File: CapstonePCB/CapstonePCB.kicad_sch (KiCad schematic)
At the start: 29 parts, among them J1 Conn_02x40_Counter_Clockwise, J2 Barrel_Jack, U1 NUCLEO64-F411RE, U2 LP-MSPM0G3507, U3 STSPIN220, U4 SN74AHC14N, U5 LM7805_TO220, U6 TLV1117-33, U8 APDS-9306

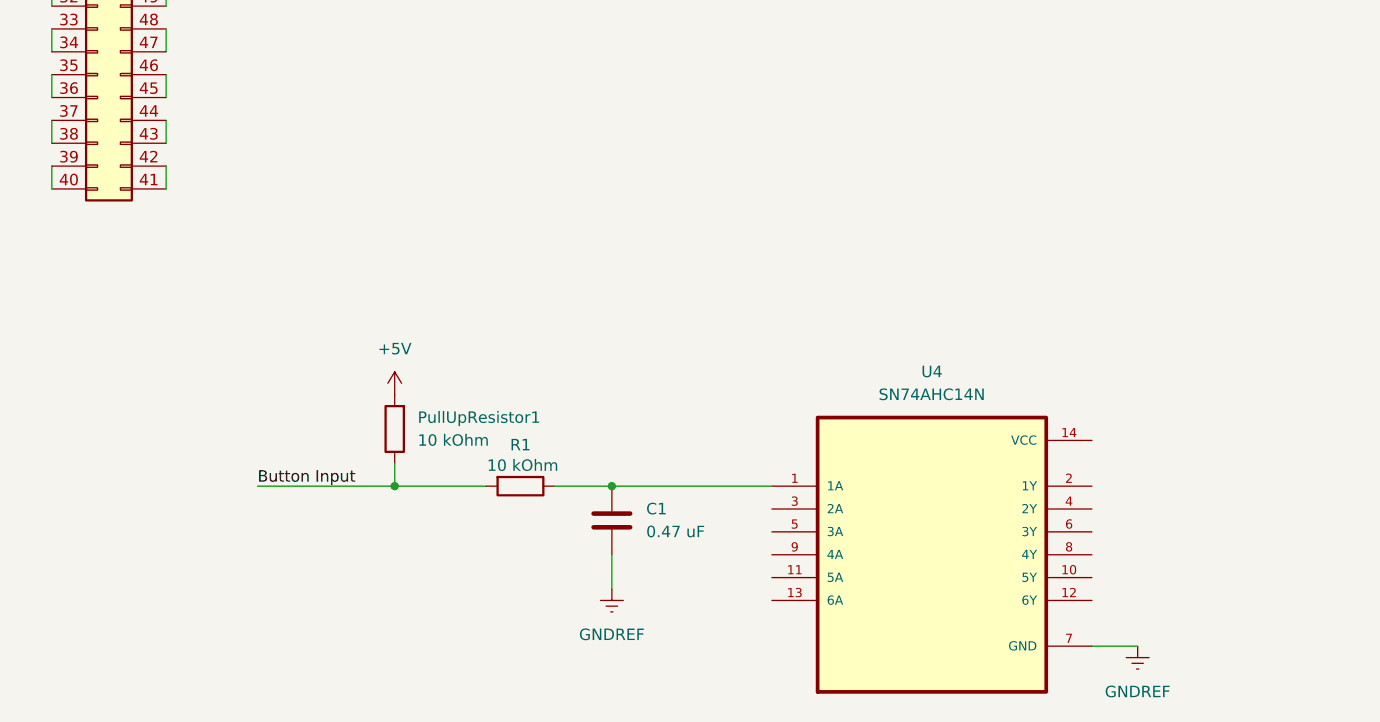
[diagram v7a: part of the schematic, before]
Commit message: Added a ground plane
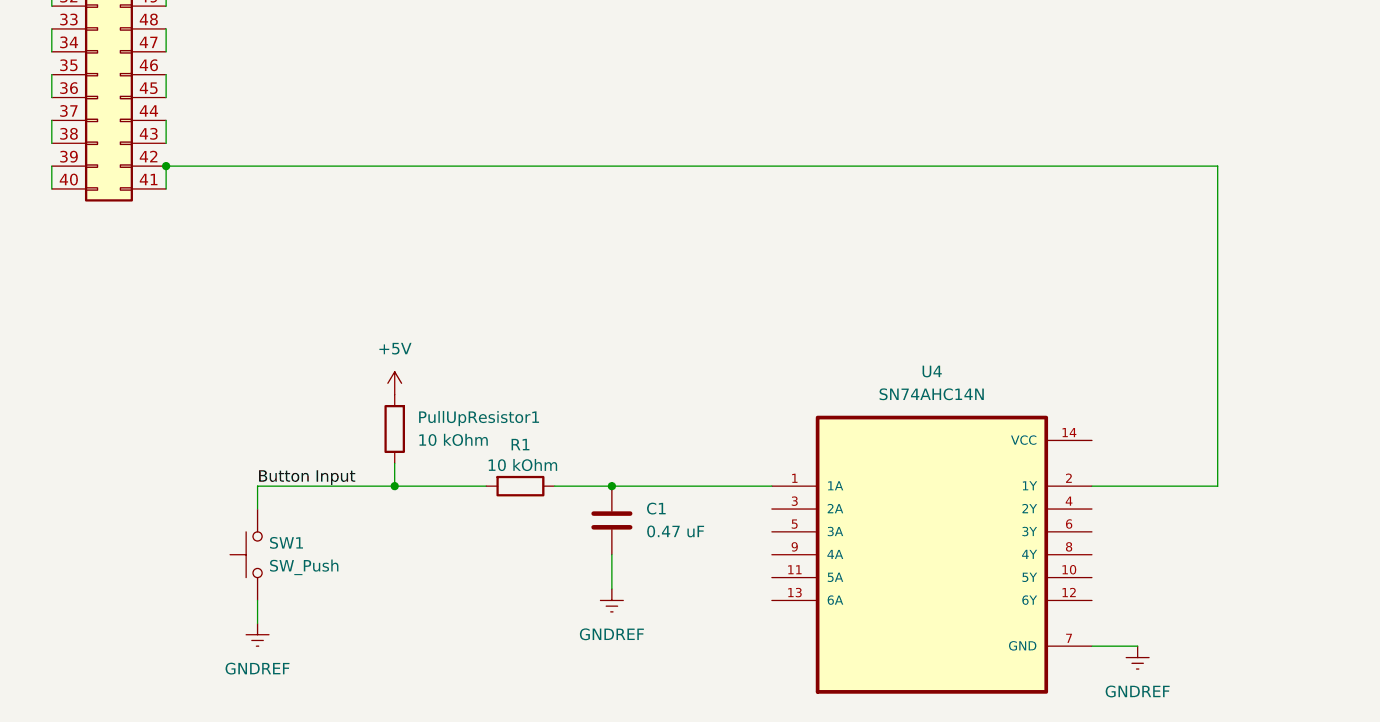
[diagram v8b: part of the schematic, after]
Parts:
- added SW1: SW_Push, Button_Switch_THT:SW_PUSH_6mm_H7.3mm, symbol Switch:SW_Push
- C1: footprint (none) -> Capacitor_SMD:C_0201_0603Metric
- PullUpResistor1, R1: footprint (none) -> Resistor_SMD:R_0201_0603Metric
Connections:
- net Button Input: now also SW1.2
- net GNDREF: now also SW1.1
- net at U4.2 (1Y): now also J1.41 (Pin_41), J1.42 (Pin_42)
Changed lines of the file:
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@@
 	)
 	(junction
+		(at 147.32 115.57)
+		(diameter 0)
+		(color 0 0 0 0)
+	)
+	(junction
 		(at 196.85 151.13)
 		(diameter 0)
@@
 	(wire
 		(pts
+			(xy 157.48 163.83) (xy 157.48 166.37)
+		)
+		(stroke
+			(width 0)
+			(type default)
+		)
+	)
+	(wire
+		(pts
 			(xy 369.57 31.75) (xy 369.57 34.29)
 		)
@@
 	(wire
 		(pts
+			(xy 250.19 151.13) (xy 264.16 151.13)
+		)
+		(stroke
+			(width 0)
+			(type default)
+		)
+	)
+	(wire
+		(pts
 			(xy 134.62 90.17) (xy 134.62 92.71)
 		)
@@
 	(wire
 		(pts
+			(xy 264.16 151.13) (xy 264.16 115.57)
+		)
+		(stroke
+			(width 0)
+			(type default)
+		)
+	)
+	(wire
+		(pts
 			(xy 172.72 148.59) (xy 172.72 151.13)
 		)
@@
 	(wire
 		(pts
+			(xy 157.48 151.13) (xy 157.48 153.67)
+		)
+		(stroke
+			(width 0)
+			(type default)
+		)
+	)
+	(wire
+		(pts
 			(xy 147.32 59.69) (xy 147.32 62.23)
 		)
@@
 	(wire
 		(pts
+			(xy 264.16 115.57) (xy 147.32 115.57)
+		)
+		(stroke
+			(width 0)
+			(type default)
+		)
+	)
+	(wire
+		(pts
 			(xy 204.47 13.97) (xy 204.47 17.78)
 		)
@@
 	)
 	(symbol
+		(lib_id "power:GNDREF")
+		(at 157.48 166.37 0)
+		(unit 1)
+		(exclude_from_sim no)
+		(in_bom yes)
+		(on_board yes)
+		(dnp no)
+		(fields_autoplaced yes)
+		(property "Reference" "#PWR030"
+			(at 157.48 172.72 0)
+			(effects
+				(font
+					(size 1.27 1.27)
+				)
+				(hide yes)
+			)
+		)
+		(property "Value" "GNDREF"
+			(at 157.48 171.45 0)
+			(effects
+				(font
+					(size 1.27 1.27)
+				)
+			)
+		)
+		(property "Footprint" ""
+			(at 157.48 166.37 0)
+			(effects
+				(font
+					(size 1.27 1.27)
+				)
+				(hide yes)
+			)
+		)
+		(property "Datasheet" ""
+			(at 157.48 166.37 0)
+			(effects
+				(font
+					(size 1.27 1.27)
+				)
+				(hide yes)
+			)
+		)
+		(property "Description" ""
+			(at 157.48 166.37 0)
+			(effects
+				(font
+					(size 1.27 1.27)
+				)
+			)
+		)
+		(pin "1"
+		)
+		(instances
+			(project "CapstonePCB"
+				(path "/39e7582f-7765-4fc9-b934-76d5b28d9065"
+					(reference "#PWR030")
+					(unit 1)
+				)
+			)
+		)
+	)
+	(symbol
 		(lib_id "Device:C_Small")
 		(at 391.16 29.21 0)
@@
 			)
 		)
-		(property "Footprint" ""
+		(property "Footprint" "Resistor_SMD:R_0201_0603Metric"
 			(at 174.498 144.78 90)
 			(effects
@@
 			)
 		)
-		(property "Footprint" ""
+		(property "Footprint" "Capacitor_SMD:C_0201_0603Metric"
 			(at 197.8152 158.75 0)
 			(effects
@@
 	)
 	(symbol
+		(lib_id "Switch:SW_Push")
+		(at 157.48 158.75 90)
+		(unit 1)
+		(exclude_from_sim no)
+		(in_bom yes)
+		(on_board yes)
+		(dnp no)
+		(fields_autoplaced yes)
+		(property "Reference" "SW1"
+			(at 158.75 157.4799 90)
+			(effects
+				(font
+					(size 1.27 1.27)
+				)
+				(justify right)
+			)
+		)
+		(property "Value" "SW_Push"
+			(at 158.75 160.0199 90)
+			(effects
+				(font
+					(size 1.27 1.27)
+				)
+				(justify right)
+			)
+		)
+		(property "Footprint" "Button_Switch_THT:SW_PUSH_6mm_H7.3mm"
+			(at 152.4 158.75 0)
+			(effects
+				(font
+					(size 1.27 1.27)
+				)
+				(hide yes)
+			)
+		)
+		(property "Datasheet" "~"
+			(at 152.4 158.75 0)
+			(effects
+				(font
+					(size 1.27 1.27)
+				)
+				(hide yes)
+			)
+		)
+		(property "Description" "Push button switch, generic, two pins"
+			(at 157.48 158.75 0)
+			(effects
+				(font
+					(size 1.27 1.27)
+				)
+				(hide yes)
+			)
+		)
+		(pin "2"
+		)
+		(pin "1"
+		)
+		(instances
+			(project ""
+				(path "/39e7582f-7765-4fc9-b934-76d5b28d9065"
+					(reference "SW1")
+					(unit 1)
+				)
+			)
+		)
+	)
+	(symbol
 		(lib_id "Device:R")
 		(at 186.69 151.13 270)
@@
 			)
 		)
-		(property "Footprint" ""
+		(property "Footprint" "Resistor_SMD:R_0201_0603Metric"
 			(at 186.69 149.352 90)
 			(effects
